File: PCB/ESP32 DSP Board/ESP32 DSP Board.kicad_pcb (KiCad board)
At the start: 6 copper layers, 88 x 66.5 mm, 89 parts, among them J1 USB4216-03-A_REVA, SW1 PTS810_SJM_250_SMTR_LFS, SW2 PTS810_SJM_250_SMTR_LFS, U8 ESP32-S3-WROOM-1, U9 TPS73733DCQ

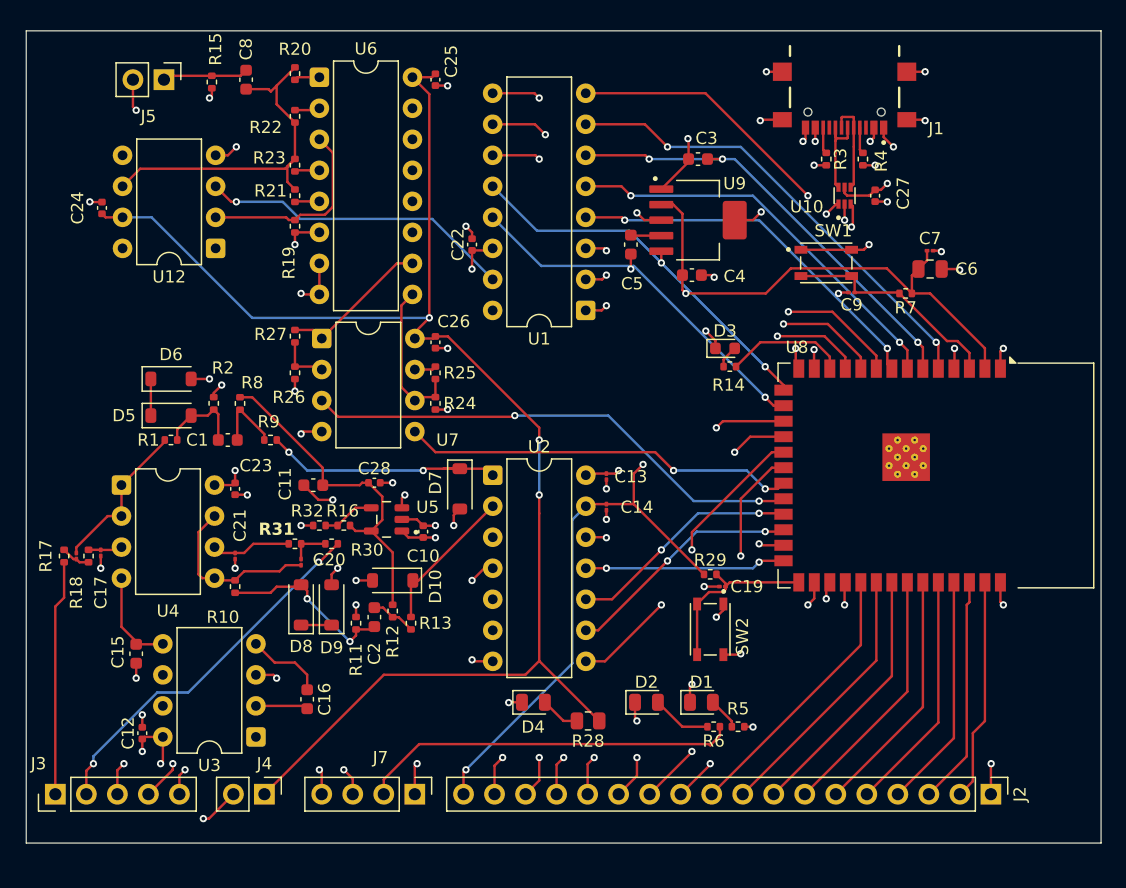
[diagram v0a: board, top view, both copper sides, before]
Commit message: Silkscreen added to connectors
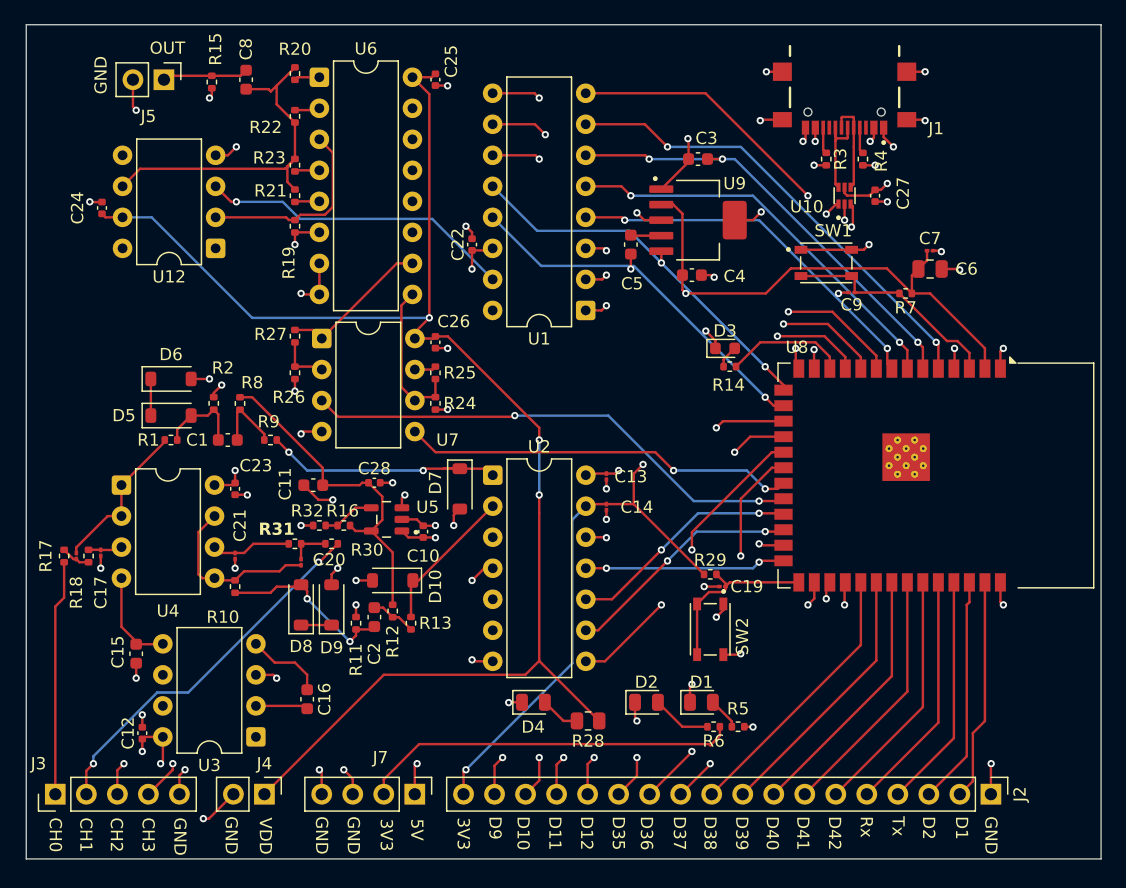
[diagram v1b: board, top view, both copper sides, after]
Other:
- board size 88 x 66.5 mm -> 88 x 68.3 mm
- board text added: "3V3"
- board text added: "5V"
- board text added: "CH0"
- board text added: "CH1"
- board text added: "CH2"
- board text added: "CH3"
- board text added: "D1"
- board text added: "D10"
- board text added: "D11"
- board text added: "D12"
- board text added: "D2"
- board text added: "D35"
- board text added: "D36"
- board text added: "D37"
- board text added: "D38"
- board text added: "D39"
- board text added: "D40"
- board text added: "D41"
- board text added: "D42"
- board text added: "D9"
- board text added: "GND"
- board text added: "OUT"
- board text added: "Rx"
- board text added: "Tx"
- board text added: "VDD"

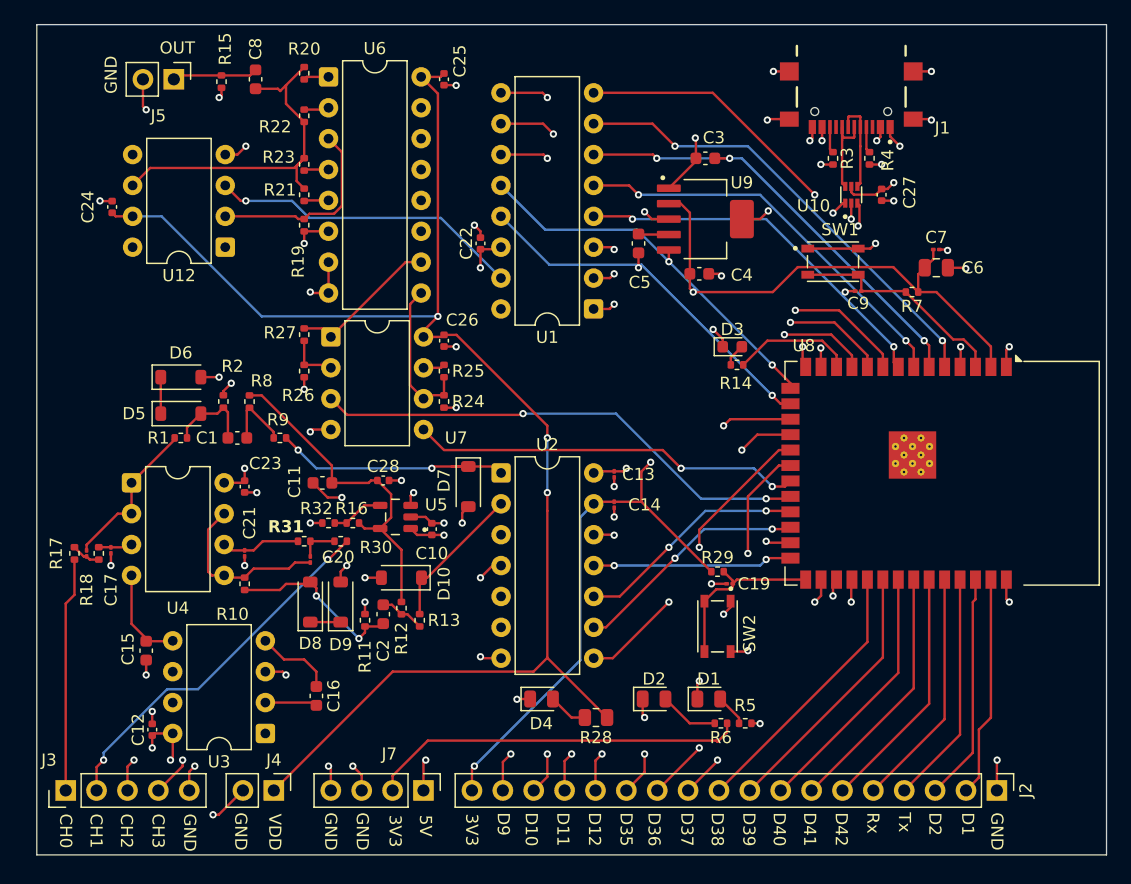
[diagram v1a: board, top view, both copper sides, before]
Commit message: Power plane split into 5V and 3V3, USB connector moved to board edge, added stitching vias
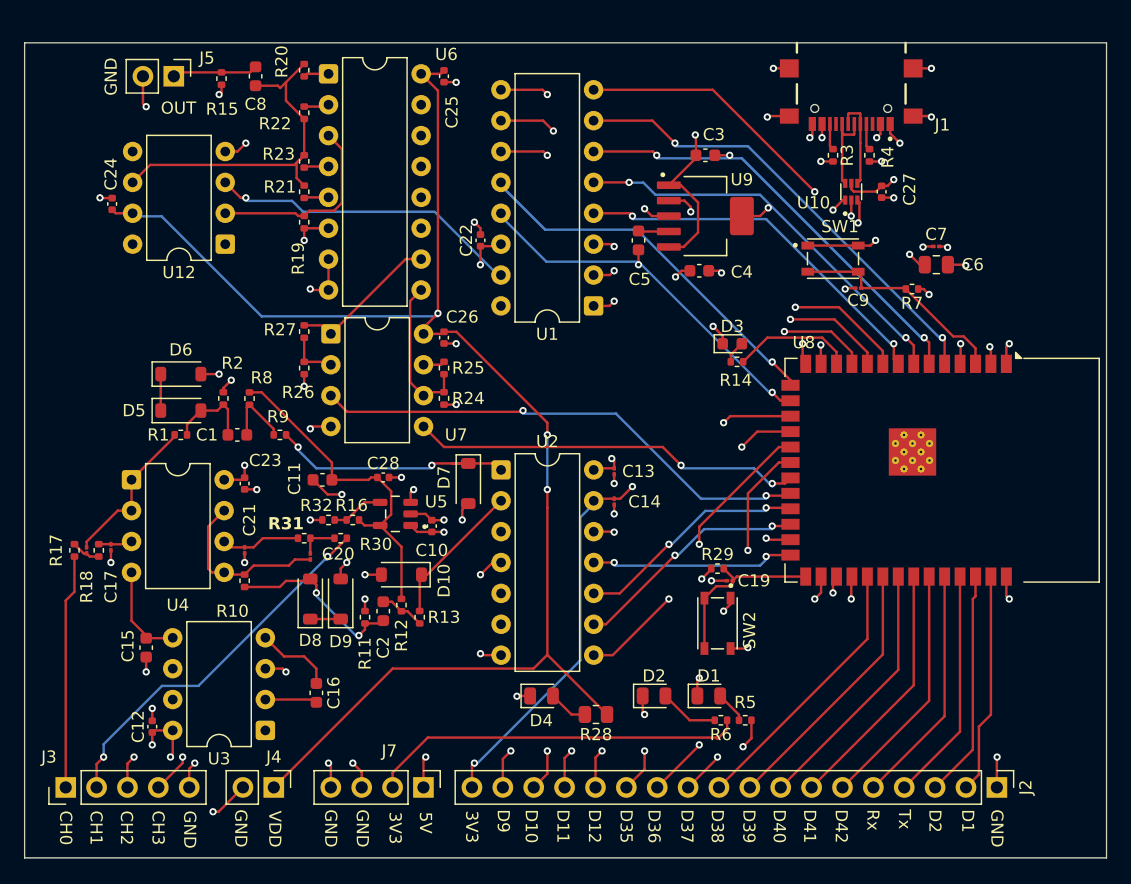
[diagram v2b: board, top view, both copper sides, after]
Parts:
- moved C1 0.25 mm to (92.5, 87.2)
- moved C10 0.25 mm to (108.5, 94.8)
- moved C11 0.25 mm to (99.5, 91.0)
- moved C12 0.25 mm to (85.5, 111.2)
- moved C13 0.25 mm to (123.5, 90.2)
- moved C14 0.25 mm to (123.5, 92.8)
- moved C15 0.25 mm to (85.0, 104.8)
- moved C16 0.25 mm to (99.0, 108.5)
- moved C17 0.25 mm to (82.1, 96.5)
- moved C18 0.25 mm to (80.1, 96.8)
- moved C19 0.25 mm to (133.0, 99.2)
- moved C2 0.25 mm to (104.5, 101.8)
- moved C20 0.25 mm to (98.5, 97.2)
- moved C21 0.25 mm to (93.1, 96.8)
- moved C22 0.25 mm to (112.5, 71.2)
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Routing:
- net +3V3: track 101.3 -> 41.6 mm, vias 3 -> 9
- net +5V: track 34.3 -> 43.2 mm, vias 14 -> 13
- net (no net): vias 0 -> 49
- added copper zone on In4.Cu, net +3V3
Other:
- board size 88 x 68.3 mm -> 89 x 67 mm

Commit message: Mounting holes added, bom and manufacturing files generated
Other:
- outline, holes or cut-outs redrawn
- board text added: "BOOT"
- board text added: "EN"
- board text added: "ESP32-S3 DSP BOARD"
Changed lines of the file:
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@@
 		(layer "Edge.Cuts")
+	)
+	(gr_circle
+		(center 162 120.05)
+		(end 162 121.05)
+		(stroke
+			(width 0.05)
+			(type default)
+		)
+		(fill no)
+		(layer "Edge.Cuts")
+	)
+	(gr_circle
+		(center 77 120.05)
+		(end 77 121.05)
+		(stroke
+			(width 0.05)
+			(type default)
+		)
+		(fill no)
+		(layer "Edge.Cuts")
+	)
+	(gr_circle
+		(center 77 57)
+		(end 78 57)
+		(stroke
+			(width 0.05)
+			(type default)
+		)
+		(fill no)
+		(layer "Edge.Cuts")
+	)
+	(gr_circle
+		(center 162 57)
+		(end 163 57)
+		(stroke
+			(width 0.05)
+			(type default)
+		)
+		(fill no)
+		(layer "Edge.Cuts")
+	)
+	(gr_text "BOOT"
+		(at 130.05 105.75 90)
+		(layer "F.SilkS")
+		(effects
+			(font
+				(size 1 1)
+				(thickness 0.1)
+			)
+			(justify left bottom)
+		)
 	)
 	(gr_text "GND"
@@
 	)
 	(gr_text "CH0"
-		(at 77.8 118.15 270)
+		(at 78.2 118.2 270)
 		(layer "F.SilkS")
 		(effects
@@
 		)
 	)
+	(gr_text "EN"
+		(at 137.3 70.7 0)
+		(layer "F.SilkS")
+		(effects
+			(font
+				(size 1 1)
+				(thickness 0.1)
+			)
+			(justify left bottom)
+		)
+	)
 	(gr_text "GND"
 		(at 82.7 59.35 90)
@@
 		(layer "F.SilkS")
 		(effects
+			(font
+				(size 1 1)
+				(thickness 0.1)
+			)
+			(justify left bottom)
+		)
+	)
+	(gr_text "ESP32-S3 DSP BOARD"
+		(at 76.55 72.85 270)
+		(layer "F.SilkS")
+		(effects

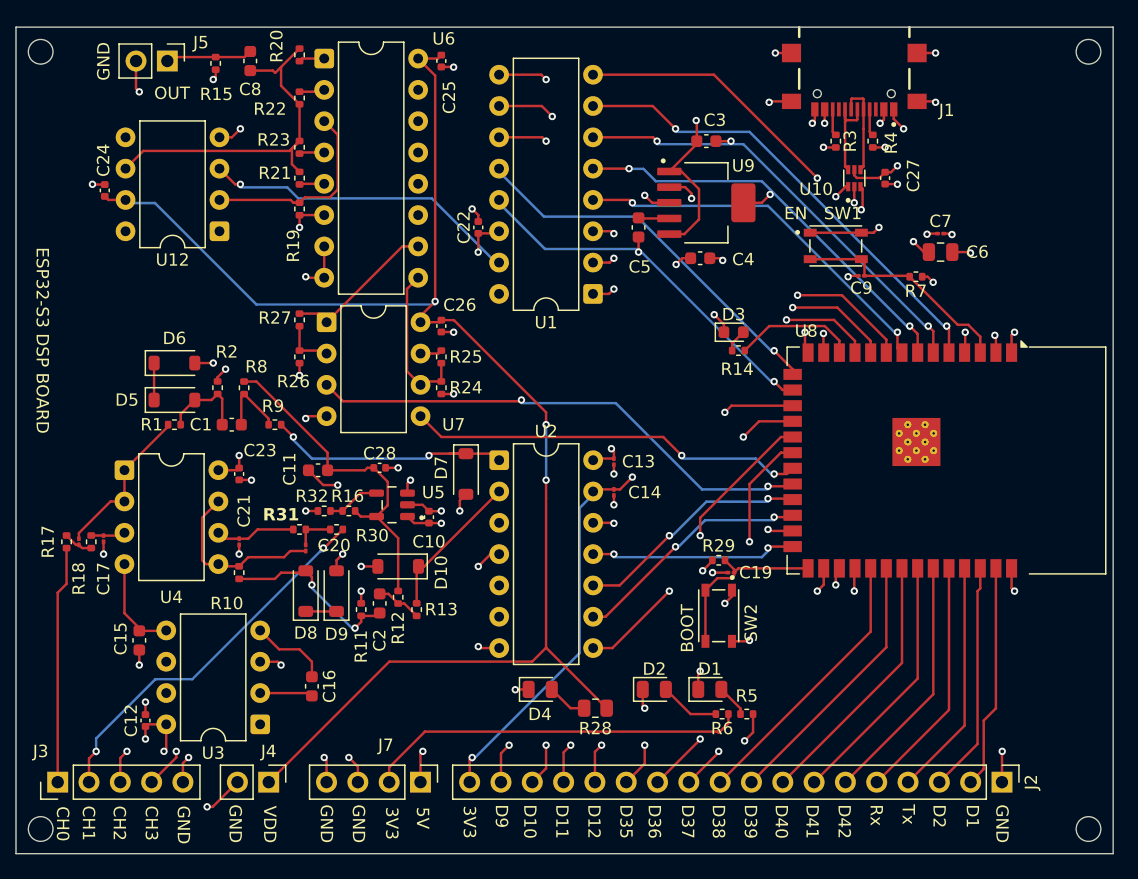
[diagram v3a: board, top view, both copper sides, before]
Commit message: all vias changed to through hole vias, production files re exported
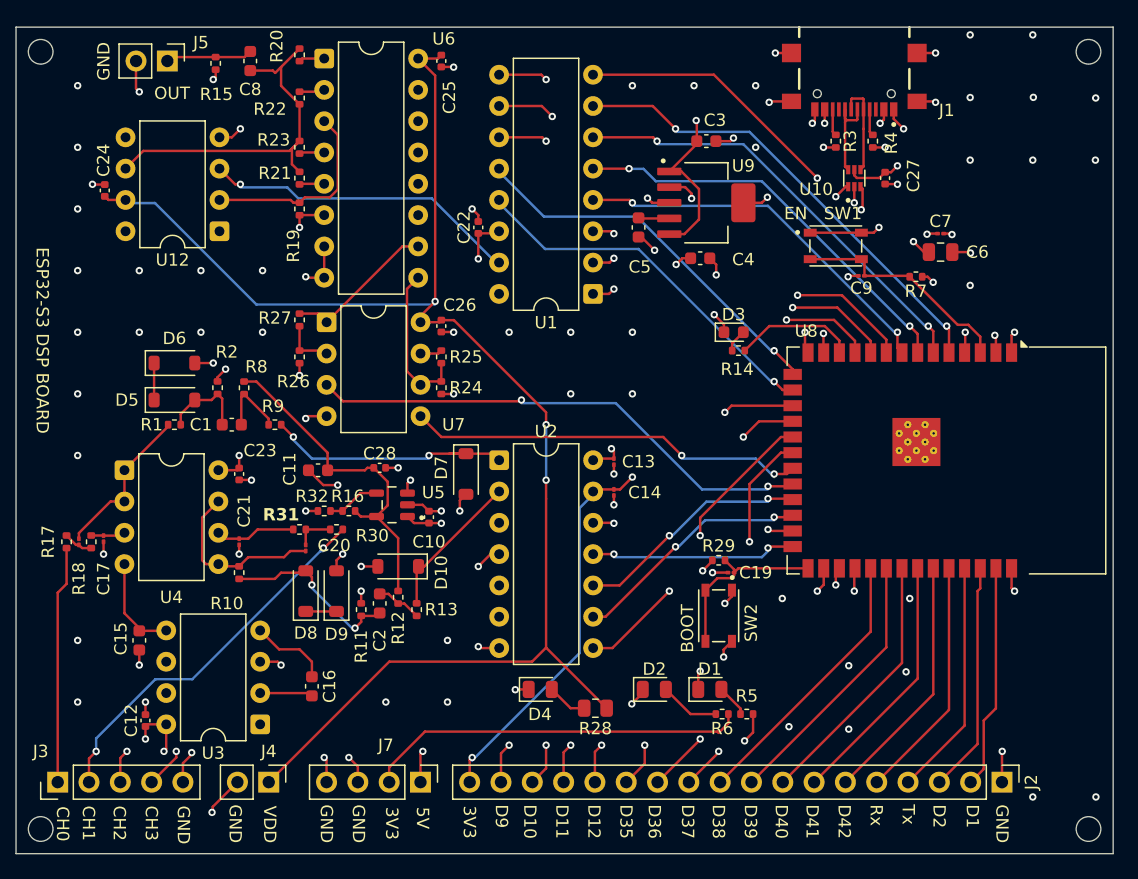
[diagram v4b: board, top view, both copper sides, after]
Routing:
- net GND: track 110.6 -> 111.8 mm
- net +5V: track 43.2 -> 43.7 mm
- net (no net): vias 49 -> 44

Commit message: Input filter altered, output amplifier fixed, 22uf decoupling added to charge pump negative output
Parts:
- moved R5 1.80 mm to (134.8, 109.0), turned to 90 degrees
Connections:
- J7 pad 2: +3.3V -> +3V3
- R6 pad 1: +3.3V -> +3V3
- U1 pad 1: GND -> +3V3
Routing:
- net +3.3V: track 31.0 -> 0.00 mm
- net +3V3: track 41.6 -> 71.3 mm, vias 9 -> 12
- net GND: track 111.8 -> 110.0 mm, vias 68 -> 67
- net +5V: track 43.7 -> 44.9 mm
- net ADC CH2: track 41.5 -> 41.9 mm, vias 1 -> 2

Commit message: Footprints changed to 1206 for resistors and capacitors, PCB restarted
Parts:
- removed D10, D5, D6, D7, D8, D9: D_Zener, Diode_SMD:D_SOD-123
- removed J1: USB4216-03-A_REVA, USB_Connector:GCT_USB4216-03-A_REVA
- removed R30, R31: 2K, Resistor_SMD:R_0402_1005Metric
- removed R32: 95.3K, Resistor_SMD:R_0402_1005Metric
- removed SW1, SW2: PTS810_SJM_250_SMTR_LFS, Switches:SW_PTS810_SJM_250_SMTR_LFS
- removed U4: ~, Package_DIP:DIP-8_W7.62mm
- removed U5: ~, LDO_Adjustable:TPS73601DBVT
- removed U9: TPS73733DCQ, LDO_3V3:TPS73733DCQ
- added C29: 47p, Capacitor_SMD:C_1206_3216Metric_Pad1.33x1.80mm_HandSolder, F.Cu at (374.8, 23.3)
- added C30: 47p, Capacitor_SMD:C_1206_3216Metric_Pad1.33x1.80mm_HandSolder, F.Cu at (374.8, 26.7)
- added U11: ~, Package_DIP:CERDIP-14_W7.62mm_SideBrazed, F.Cu at (351.7, 56.5)
- C1: value 10uF -> 0.1uF; footprint Capacitor_SMD:C_0603_1608Metric -> Capacitor_SMD:C_1206_3216Metric_Pad1.33x1.80mm_HandSolder
- C10, C23: value 0.1uF -> 47p; footprint Capacitor_SMD:C_0402_1005Metric -> Capacitor_SMD:C_1206_3216Metric_Pad1.33x1.80mm_HandSolder
- C11, C2: value 10uF -> 47p; footprint Capacitor_SMD:C_0603_1608Metric -> Capacitor_SMD:C_1206_3216Metric_Pad1.33x1.80mm_HandSolder
- C12, C22, C24, C25, C26, C27: footprint Capacitor_SMD:C_0402_1005Metric -> Capacitor_SMD:C_1206_3216Metric_Pad1.33x1.80mm_HandSolder
- C13, C14, C19, C7, C9: footprint Capacitor_SMD:C_01005_0402Metric -> Capacitor_SMD:C_1206_3216Metric_Pad1.33x1.80mm_HandSolder
- C15: value 10uF -> 22uF; footprint Capacitor_SMD:C_0603_1608Metric -> Capacitor_THT:CP_Radial_Tantal_D4.5mm_P2.50mm
- C16, C3, C4, C5: footprint Capacitor_SMD:C_0603_1608Metric -> Capacitor_SMD:C_1206_3216Metric_Pad1.33x1.80mm_HandSolder
- C17, C18, C20, C21: value 100p -> 47p; footprint Capacitor_SMD:C_01005_0402Metric -> Capacitor_SMD:C_1206_3216Metric_Pad1.33x1.80mm_HandSolder
- C28: value 10nF -> 47p; footprint Capacitor_SMD:C_0402_1005Metric -> Capacitor_SMD:C_1206_3216Metric_Pad1.33x1.80mm_HandSolder
- C6: footprint Capacitor_SMD:C_0805_2012Metric -> Capacitor_SMD:C_1206_3216Metric_Pad1.33x1.80mm_HandSolder
- C8: value 1uF -> 47p; footprint Capacitor_SMD:C_0603_1608Metric -> Capacitor_SMD:C_1206_3216Metric_Pad1.33x1.80mm_HandSolder
- R1, R10, R11, R12, R13, R2, R8, R9: value 10K -> 33K; footprint Resistor_SMD:R_0402_1005Metric -> Resistor_SMD:R_1206_3216Metric_Pad1.30x1.75mm_HandSolder
- R14, R20, R24, R25, R26, R27, R29, R3, R4, R5, R6, R7: footprint Resistor_SMD:R_0402_1005Metric -> Resistor_SMD:R_1206_3216Metric_Pad1.30x1.75mm_HandSolder
- R15: value 1K -> 33K; footprint Resistor_SMD:R_0402_1005Metric -> Resistor_SMD:R_1206_3216Metric_Pad1.30x1.75mm_HandSolder
- R16: value 23.2K -> 33K; footprint Resistor_SMD:R_0402_1005Metric -> Resistor_SMD:R_1206_3216Metric_Pad1.30x1.75mm_HandSolder
- R17, R18: value 2K -> 33K; footprint Resistor_SMD:R_0402_1005Metric -> Resistor_SMD:R_1206_3216Metric_Pad1.30x1.75mm_HandSolder
- R19, R21: value 10K -> 5.1K; footprint Resistor_SMD:R_0402_1005Metric -> Resistor_SMD:R_1206_3216Metric_Pad1.30x1.75mm_HandSolder
- R22: value 15K -> 11K; footprint Resistor_SMD:R_0402_1005Metric -> Resistor_SMD:R_1206_3216Metric_Pad1.30x1.75mm_HandSolder
- R23: value 22K -> 20K; footprint Resistor_SMD:R_0402_1005Metric -> Resistor_SMD:R_1206_3216Metric_Pad1.30x1.75mm_HandSolder
- R28: footprint Resistor_SMD:R_0805_2012Metric -> Resistor_SMD:R_1206_3216Metric_Pad1.30x1.75mm_HandSolder
- moved J3 301.6 mm to (373.9, 56.1), turned to 0 degrees
- moved C18 300.5 mm to (368.8, 13.3), turned to 0 degrees
- moved C12 290.9 mm to (362.8, 23.3), turned to 0 degrees
- moved C24 288.7 mm to (368.8, 33.4), turned to 0 degrees
- moved C17 287.0 mm to (362.8, 36.7), turned to 0 degrees
- moved C21 285.3 mm to (368.8, 23.3), turned to 0 degrees
- moved C23 282.4 mm to (368.8, 30.0), turned to 0 degrees
- moved U12 281.8 mm to (373.2, 76.5), turned to 0 degrees
- moved C20 281.1 mm to (368.8, 20.0), turned to 0 degrees
- moved C15 281.0 mm to (365.6, 89.2), turned to 0 degrees
- moved C28 279.4 mm to (374.8, 20.0)
- moved J7 277.3 mm to (378.5, 56.1), turned to 0 degrees
- moved J5 275.9 mm to (361.4, 88.5), turned to 0 degrees
- moved C1 274.4 mm to (356.8, 13.3)
- moved C16 274.3 mm to (362.8, 33.4), turned to 0 degrees
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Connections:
- C1 pad 1: Net-(D5-A) -> +5V
- C1 pad 2: Net-(C1-Pad2) -> GND
- C10 pad 1: GND -> Net-(U11-+InD)
- C10 pad 2: +5V -> GND
- C11 pad 1: 1.5V -> Net-(C11-Pad1)
- C17 pad 1: Net-(U4-1IN+) -> Net-(C17-Pad1)
- C17 pad 2: GND -> CH1_FOUT
- C18 pad 1: Net-(C18-Pad1) -> Net-(U11-+InC)
- C18 pad 2: CH0_FOUT -> GND
- C2 pad 1: Net-(D8-A) -> Net-(C2-Pad1)
- C2 pad 2: Net-(C2-Pad2) -> GND
- C20 pad 2: CH1_FOUT -> GND
- C21 pad 1: Net-(U4-2IN-) -> Net-(C21-Pad1)
- C21 pad 2: GND -> CH2_FOUT
- C23 pad 1: +5V -> Net-(U11-+InB)
- C28 pad 1: 1.5V -> GND
- C28 pad 2: GND -> Net-(C28-Pad2)
- C8 pad 1: Net-(C8-Pad1) -> CH0_FOUT
- C8 pad 2: Net-(U12-OUT) -> Net-(C8-Pad2)
- J5 pad 1: Net-(C8-Pad1) -> Net-(U12-OUT)
- R1 pad 1: CH0_FOUT -> Net-(C2-Pad1)
- R1 pad 2: Net-(D5-A) -> ADC CH0
- R10 pad 1: CH1_FOUT -> Net-(C17-Pad1)
- R10 pad 2: Net-(D8-A) -> Net-(C11-Pad1)
- R11 pad 1: Net-(D8-A) -> Net-(U11-+InC)
- R11 pad 2: GND -> Net-(C17-Pad1)
- R12 pad 1: Net-(C2-Pad2) -> ADC CH2
- R12 pad 2: 1.5V -> Net-(C20-Pad1)
- R13 pad 1: Net-(C2-Pad2) -> Net-(C20-Pad1)
- R13 pad 2: CH1 IN -> Net-(C21-Pad1)
- R15 pad 1: Net-(C8-Pad1) -> Net-(C21-Pad1)
- R15 pad 2: GND -> Net-(U11-+InB)
- R16 pad 1: 1.5V -> ADC CH3
- R16 pad 2: Net-(U5-NR/FB) -> Net-(C28-Pad2)
- R17 pad 1: Net-(C18-Pad1) -> Net-(C28-Pad2)
- R17 pad 2: ADC CH0 -> Net-(C29-Pad2)
- R18 pad 1: Net-(U4-1IN+) -> Net-(C29-Pad2)
- R18 pad 2: Net-(C18-Pad1) -> Net-(U11-+InA)
- R2 pad 1: Net-(D5-A) -> Net-(C8-Pad2)
- R2 pad 2: GND -> Net-(C2-Pad1)
- R24 pad 1: 2B -> Net-(U7-2IN-)
- R25 pad 1: 2B -> Net-(U7-2IN-)
- R25 pad 2: Net-(U7-2OUT) -> 2B
- R8 pad 1: Net-(C1-Pad2) -> Net-(U11-+InD)
- R8 pad 2: 1.5V -> Net-(C8-Pad2)
- R9 pad 1: Net-(C1-Pad2) -> Net-(C11-Pad1)
- R9 pad 2: CH0 IN -> ADC CH1
- U2 pad 1: CH0 IN -> CH0_FOUT
- U2 pad 2: CH1 IN -> CH1_FOUT
- U2 pad 3: ADC CH2 -> CH2_FOUT
- U2 pad 4: ADC CH3 -> CH3_FOUT
- U7 pad 6: 2B -> Net-(U7-2IN-)
- U7 pad 7: Net-(U7-2OUT) -> 2B
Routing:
- net VDD: track 121.7 -> 0.00 mm, vias 3 -> 0
- net GND: track 110.0 -> 0.00 mm, vias 67 -> 0
- net +3V3: track 71.3 -> 0.00 mm, vias 12 -> 0
- net +5V: track 44.9 -> 0.00 mm, vias 13 -> 0
- net A: track 41.4 -> 0.00 mm, vias 2 -> 0
- net DB4: track 38.3 -> 0.00 mm, vias 2 -> 0
- net DB5: track 35.9 -> 0.00 mm, vias 2 -> 0
- net DB6: track 33.5 -> 0.00 mm, vias 2 -> 0
- net B: track 32.3 -> 0.00 mm, vias 2 -> 0
- net CS': track 31.0 -> 0.00 mm, vias 1 -> 0
- net ADC CH1: track 31.0 -> 0.00 mm, vias 2 -> 0
- net DB7: track 30.9 -> 0.00 mm, vias 2 -> 0
- net WR': track 30.2 -> 0.00 mm, vias 1 -> 0
- net Net-(U12-OUT): track 29.6 -> 0.00 mm
- net 1.5V: track 27.9 -> 0.00 mm
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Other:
- board size 89 x 67 mm -> 165.8 x 86 mm
- board text removed: "3V3"
- board text removed: "5V"
- board text removed: "BOOT"
- board text removed: "CH0"
- board text removed: "CH1"
- board text removed: "CH2"
- board text removed: "CH3"
- board text removed: "D1"
- board text removed: "D10"
- board text removed: "D11"
- board text removed: "D12"
- board text removed: "D2"
- board text removed: "D35"
- board text removed: "D36"
- board text removed: "D37"
- board text removed: "D38"
- board text removed: "D39"
- board text removed: "D40"
- board text removed: "D41"
- board text removed: "D42"
- board text removed: "D9"
- board text removed: "EN"
- board text removed: "ESP32-S3 DSP BOARD"
- board text removed: "GND"
- board text removed: "OUT"
- board text removed: "Rx"
- board text removed: "Tx"
- board text removed: "VDD"
